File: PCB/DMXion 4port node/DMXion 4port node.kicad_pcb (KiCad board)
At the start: 4 copper layers, 100 x 100 mm, 257 parts, among them IC1 NPM1300-QEAA-R7, J1 Conn_01x03_MountingPin, J10 XLR5, J11 XLR3, J12 IDC, J13 Conn_02x04, J2 USB_C_Receptacle_USB2.0_14P, J3 RJ45, J4 XLR5, J5 XLR3, J6 XLR5, J7 XLR3, J8 XLR5, J9 XLR3, SW1 SW_Push, SW2 SW_Push, T1 FA2805, U1 RP2350B, U10 MAX3485, U11 MAX3485, U12 TXS0101DCK, U13 AP7361C-33E, U2 W25Q128JVS, U3 USBLC6-2SC6, U4 W5500, U5 VO618A-3X019T, U6 SI3402-B-GMR, U7 TLV431, U8 MAX3485, U9 MAX3485, Y1 ABM8-272-T3, Y2 ABM8-25.000MHZ-10-D1G-T

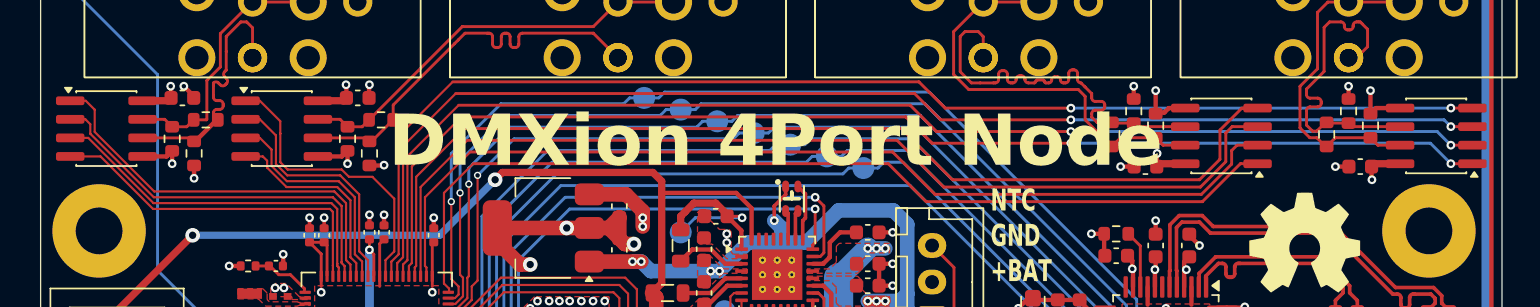
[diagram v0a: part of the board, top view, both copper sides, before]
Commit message: Added more testpoints
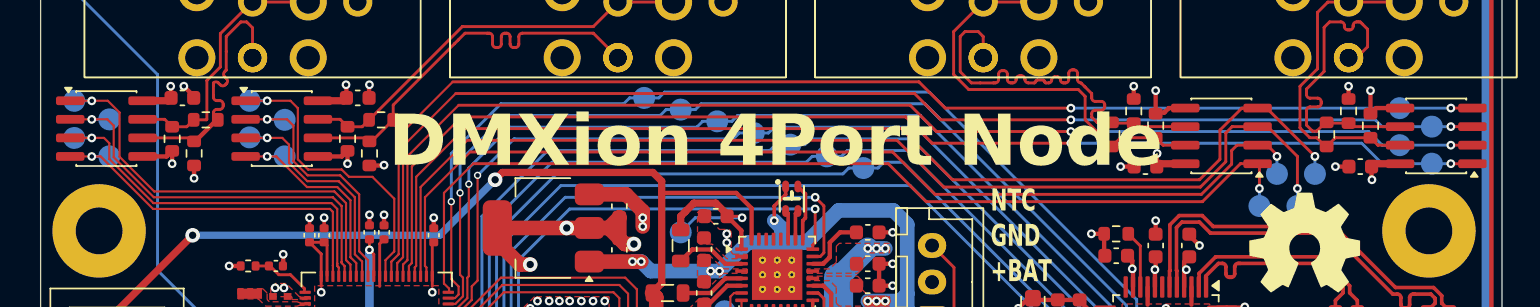
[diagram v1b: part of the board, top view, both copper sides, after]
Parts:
- added TP45: TestPoint, TestPoint:TestPoint_Pad_D1.5mm, B.Cu at (135.2, 63.4)
- added TP46: TestPoint, TestPoint:TestPoint_Pad_D1.5mm, B.Cu at (135.2, 60.9)
- added TP47: TestPoint, TestPoint:TestPoint_Pad_D1.5mm, B.Cu at (133.0, 59.6)
- added TP48: TestPoint, TestPoint:TestPoint_Pad_D1.5mm, B.Cu at (133.0, 62.1)
- added TP49: TestPoint, TestPoint:TestPoint_Pad_D1.5mm, B.Cu at (123.4, 66.3)
- added TP50: TestPoint, TestPoint:TestPoint_Pad_D1.5mm, B.Cu at (124.6, 64.1)
- added TP51: TestPoint, TestPoint:TestPoint_Pad_D1.5mm, B.Cu at (126.0, 66.3)
- added TP52: TestPoint, TestPoint:TestPoint_Pad_D1.5mm, B.Cu at (127.2, 64.1)
- added TP53: TestPoint, TestPoint:TestPoint_Pad_D1.5mm, B.Cu at (54.3, 59.1)
- added TP54: TestPoint, TestPoint:TestPoint_Pad_D1.5mm, B.Cu at (56.7, 60.4)
- added TP55: TestPoint, TestPoint:TestPoint_Pad_D1.5mm, B.Cu at (54.3, 61.6)
- added TP56: TestPoint, TestPoint:TestPoint_Pad_D1.5mm, B.Cu at (56.7, 62.9)
- added TP57: TestPoint, TestPoint:TestPoint_Pad_D1.5mm, B.Cu at (42.3, 59.1)
- added TP58: TestPoint, TestPoint:TestPoint_Pad_D1.5mm, B.Cu at (44.7, 60.4)
- added TP59: TestPoint, TestPoint:TestPoint_Pad_D1.5mm, B.Cu at (42.3, 61.6)
- added TP60: TestPoint, TestPoint:TestPoint_Pad_D1.5mm, B.Cu at (44.7, 62.9)
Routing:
- net /DMX/DMX_2_EN: track 68.8 -> 75.8 mm, vias 0 -> 1
- net /DMX/DMX_2_OUT: track 70.4 -> 76.9 mm, vias 0 -> 1
- net /DMX/DMX_2_RDM: track 65.6 -> 68.6 mm, vias 0 -> 1
- net /DMX/2_RDM_EN: track 66.8 -> 69.7 mm, vias 0 -> 1
- net /DMX/4_RDM_EN: track 26.2 -> 28.3 mm, vias 0 -> 1
- net /DMX/DMX_4_RDM: track 27.7 -> 29.8 mm, vias 0 -> 1
- net /DMX/DMX_4_EN: track 24.9 -> 26.7 mm, vias 0 -> 1
- net /DMX/DMX_3_RDM: track 20.1 -> 21.7 mm, vias 0 -> 1
- net /DMX/3_RDM_EN: track 16.8 -> 18.3 mm, vias 0 -> 1
- net /DMX/DMX_3_EN: track 15.4 -> 16.7 mm, vias 0 -> 1
- net /DMX/DMX_4_OUT: track 23.9 -> 25.1 mm, vias 0 -> 1
- net /DMX/DMX_3_OUT: track 14.0 -> 14.9 mm, vias 0 -> 1

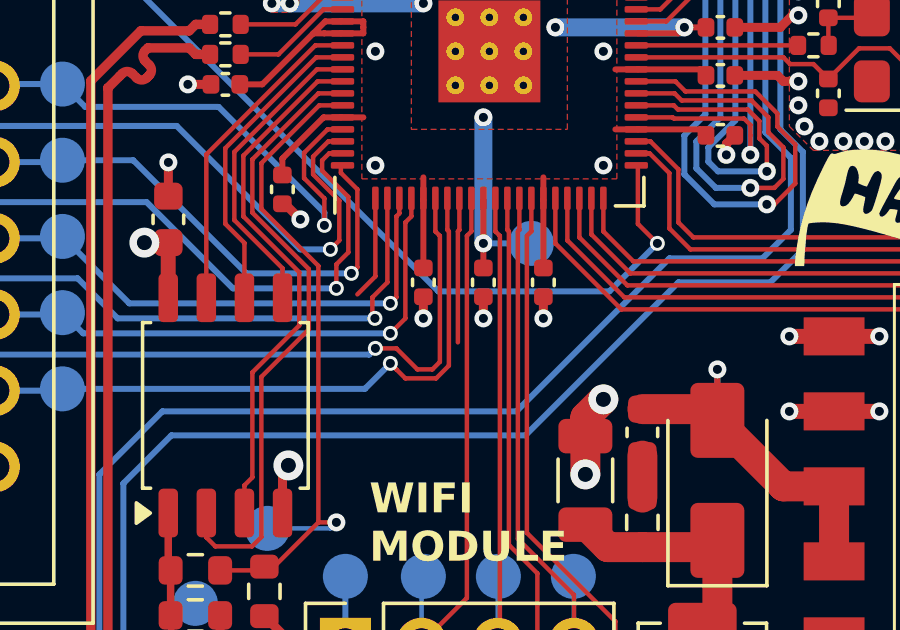
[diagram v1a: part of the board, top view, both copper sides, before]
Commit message: Even more testpads
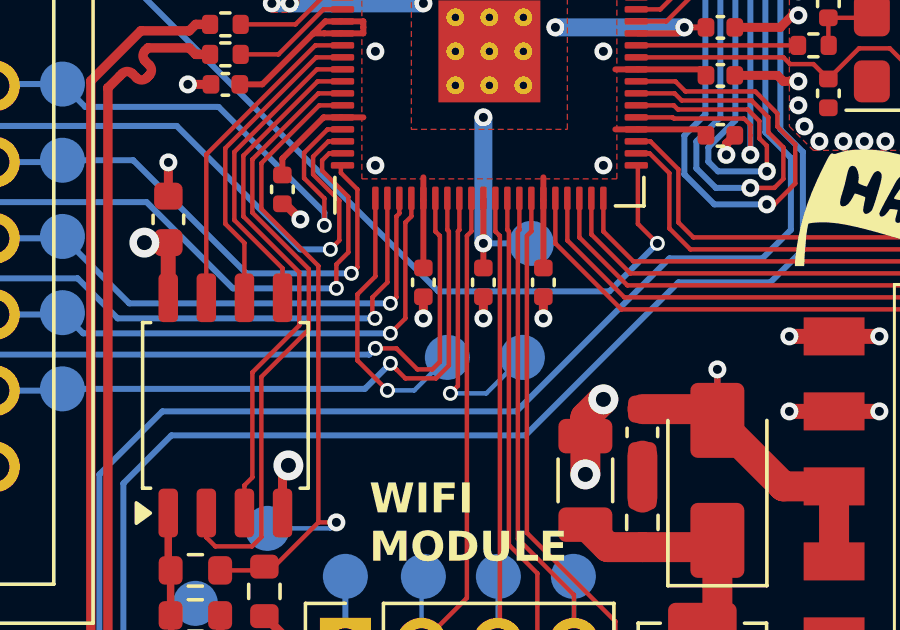
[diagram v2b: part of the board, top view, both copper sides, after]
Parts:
- added TP61: TestPoint, TestPoint:TestPoint_Pad_D1.5mm, B.Cu at (61.6, 86.2)
- added TP62: TestPoint, TestPoint:TestPoint_Pad_D1.5mm, B.Cu at (64.1, 86.2)
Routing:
- net /Microcontroller/GPIO4: track 3.40 -> 9.47 mm, vias 0 -> 1
- net /Microcontroller/GPIO10: track 4.77 -> 9.47 mm, vias 0 -> 1

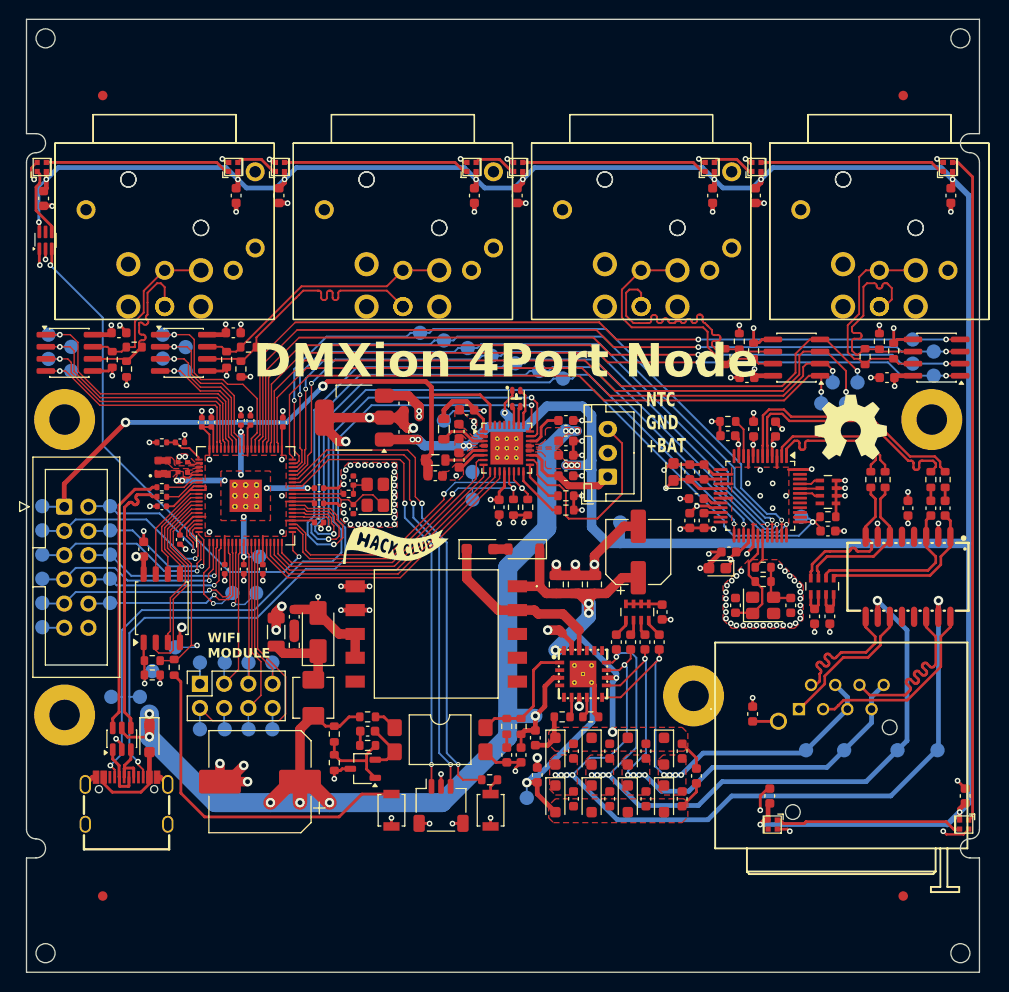
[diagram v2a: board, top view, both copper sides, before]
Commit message: Fixed allot of PCB mistakes and added more silkscreen
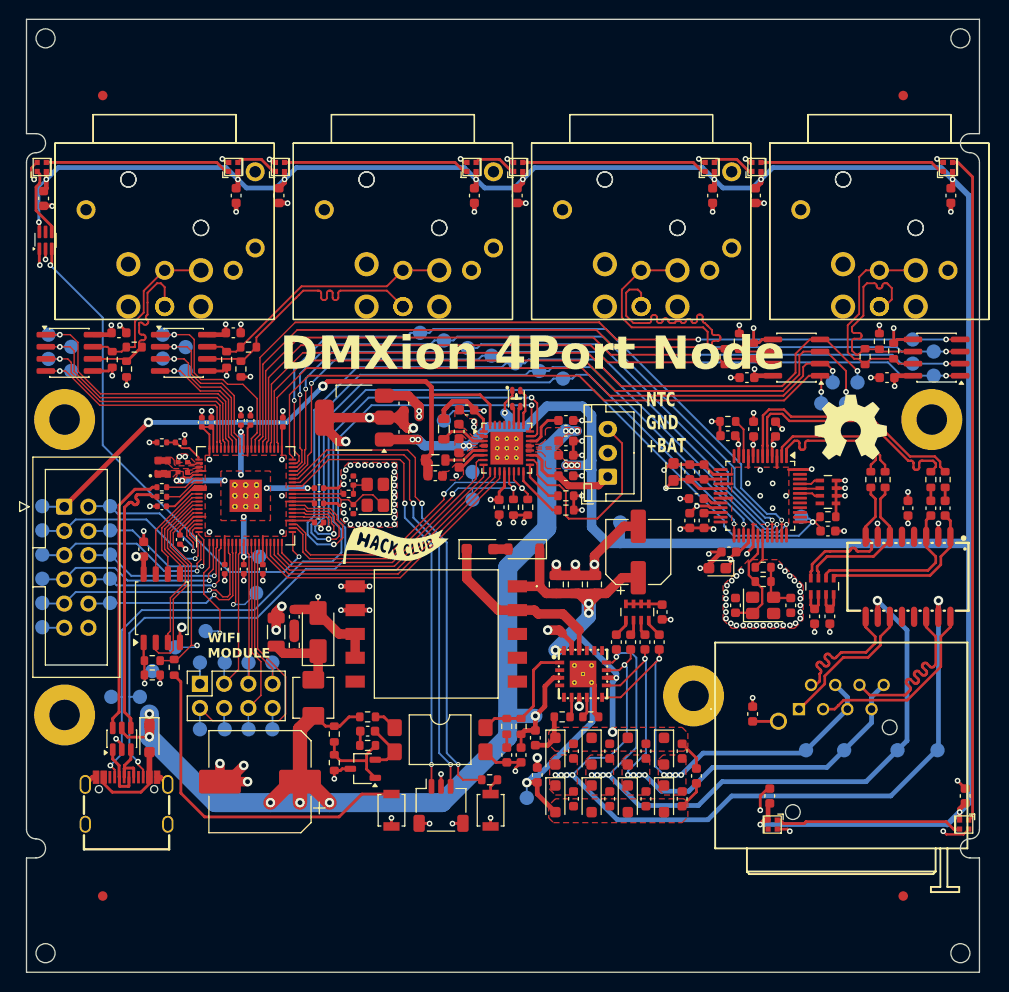
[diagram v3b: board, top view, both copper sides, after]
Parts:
- moved TP61 4.88 mm to (58.8, 90.2)
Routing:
- net /Microcontroller/GPIO4: track 9.47 -> 12.0 mm
- net +3V3: track 109.5 -> 111.4 mm
- net +DISPLAY: track 66.4 -> 64.9 mm
- net /Ethernet/V+: track 50.5 -> 51.2 mm
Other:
- board text added: "https://github.com/NEOgHacking/DMXion_4Port_Node"
